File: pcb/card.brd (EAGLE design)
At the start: 84.8 x 54 mm, 22 parts, among them IC1 74HC14D, IC2 24LC256SN, Q1 BC817

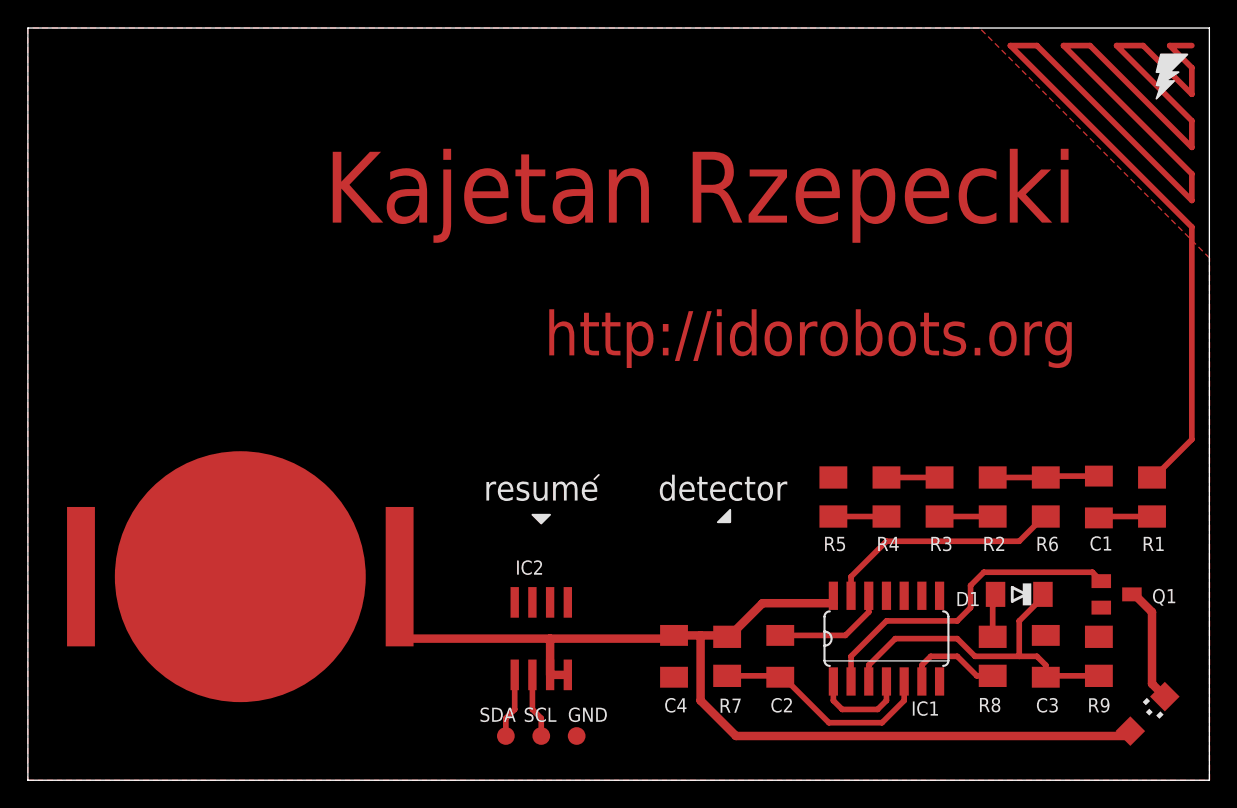
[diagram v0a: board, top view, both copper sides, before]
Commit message: Added a centigrade measure to the PCB edge.
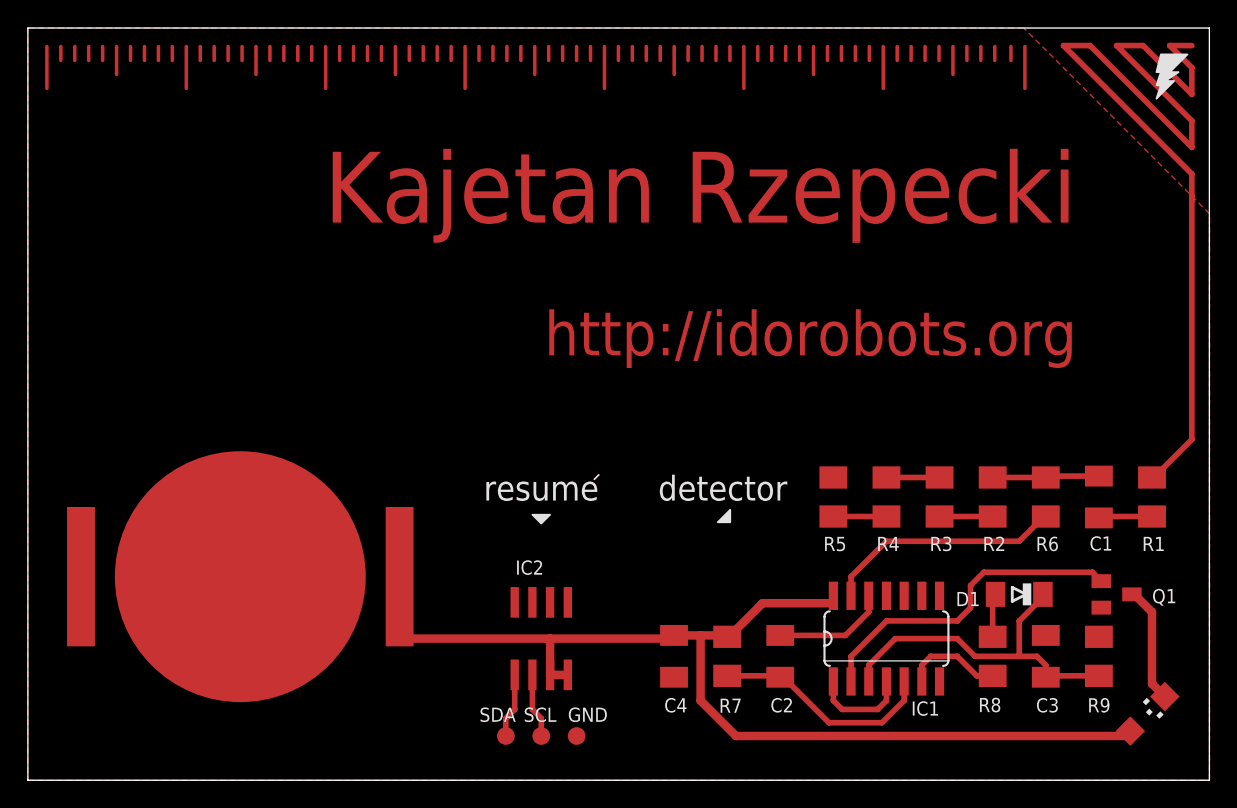
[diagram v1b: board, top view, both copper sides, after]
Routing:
- net ANT: track 104.7 -> 70.6 mm
- net N$87: track 0.00 -> 3.00 mm
- net N$77: track 0.00 -> 3.00 mm
- net N$67: track 0.00 -> 3.00 mm
- net N$57: track 0.00 -> 3.00 mm
- net N$47: track 0.00 -> 3.00 mm
- net N$37: track 0.00 -> 3.00 mm
- net N$27: track 0.00 -> 3.00 mm
- net N$17: track 0.00 -> 3.00 mm
- net N$82: track 0.00 -> 2.00 mm
- net N$72: track 0.00 -> 2.00 mm
- net N$62: track 0.00 -> 2.00 mm
- net N$52: track 0.00 -> 2.00 mm
- net N$42: track 0.00 -> 2.00 mm
- net N$32: track 0.00 -> 2.00 mm
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
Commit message: Swapped I2C EEPROM for SPI Flash & adjusted the design accordingly.
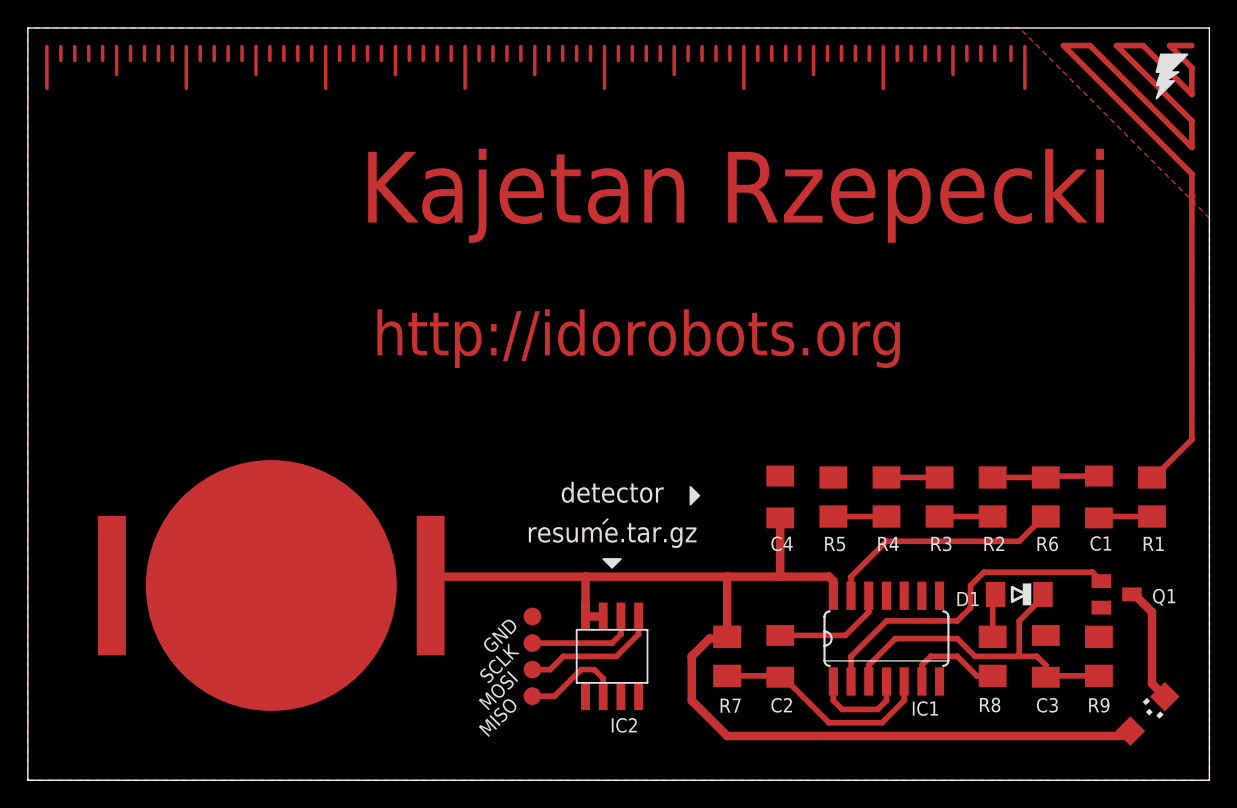
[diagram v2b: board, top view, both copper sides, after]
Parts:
- removed SCL, SDA: TPB1,27, testpad:B1,27
- added MISO, MOSI, SCLK: TPB1,27, testpad:B1,27
- IC2: value 24LC256SN -> W25X32; device microchip:SO-08 -> bat:SOIC8
- moved C4 13.7 mm to (54.0, 20.3), turned to 270 degrees
- moved GND 9.14 mm to (36.2, 11.7), turned to 90 degrees
- moved IC2 5.85 mm to (42.5, 8.89), turned to 90 degrees
- moved BAT 2.31 mm to (17.5, 14.0)
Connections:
- new net N$88: IC2.2, MISO.TP
- net GND: no longer IC2.2
- net N$10: now also IC2.6, SCLK.TP; no longer IC2.5, SDA.TP
- net N$9: now also IC2.5, MOSI.TP; no longer IC2.6, SCL.TP
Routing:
- net N$88: track 0.00 -> 7.40 mm
- net N$9: track 4.65 -> 9.94 mm
- net VCC: track 80.0 -> 83.6 mm
- net N$10: track 4.65 -> 7.88 mm
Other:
- board text added: "resume.tar.gz"
- board text removed: "resume"

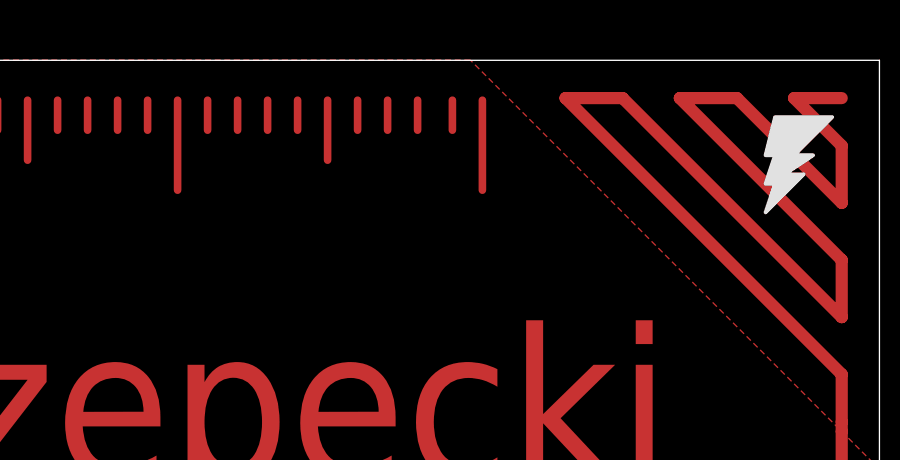
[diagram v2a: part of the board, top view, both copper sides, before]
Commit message: Fixed misaligned centigrade measure wires.
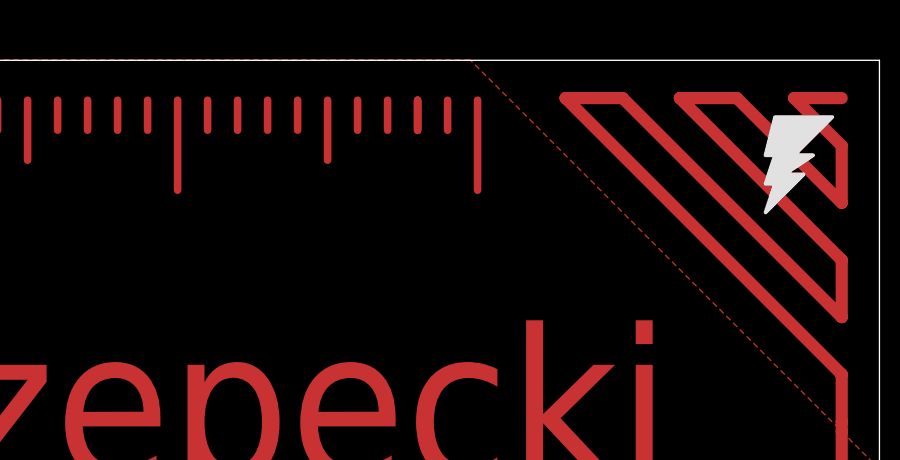
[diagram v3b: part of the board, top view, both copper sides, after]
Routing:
- net N$90: track 0.00 -> 1.00 mm
- net N$89: track 0.00 -> 1.00 mm
- net N$86: track 1.00 -> 0.00 mm
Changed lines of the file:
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@@
 <wire x1="69.365" y1="52.635" x2="69.365" y2="51.635" width="0.254" layer="1"/>
 </signal>
-<signal name="N$86">
-<wire x1="70.525" y1="52.635" x2="70.525" y2="51.635" width="0.254" layer="1"/>
-</signal>
 <signal name="N$87">
-<wire x1="71.525" y1="52.635" x2="71.525" y2="49.635" width="0.254" layer="1"/>
+<wire x1="71.36384375" y1="52.635" x2="71.36384375" y2="49.635" width="0.254" layer="1"/>
 </signal>
 <signal name="N$10">
@@
 <wire x1="37.7825" y1="6.0325" x2="36.195" y2="6.0325" width="0.4064" layer="1"/>
 </signal>
+<signal name="N$89">
+<wire x1="69.3651875" y1="52.633190625" x2="69.3651875" y2="51.633190625" width="0.254" layer="1"/>
+</signal>
+<signal name="N$90">
+<wire x1="70.3651875" y1="51.633190625" x2="70.3651875" y2="52.633190625" width="0.254" layer="1"/>
+</signal>
 </signals>

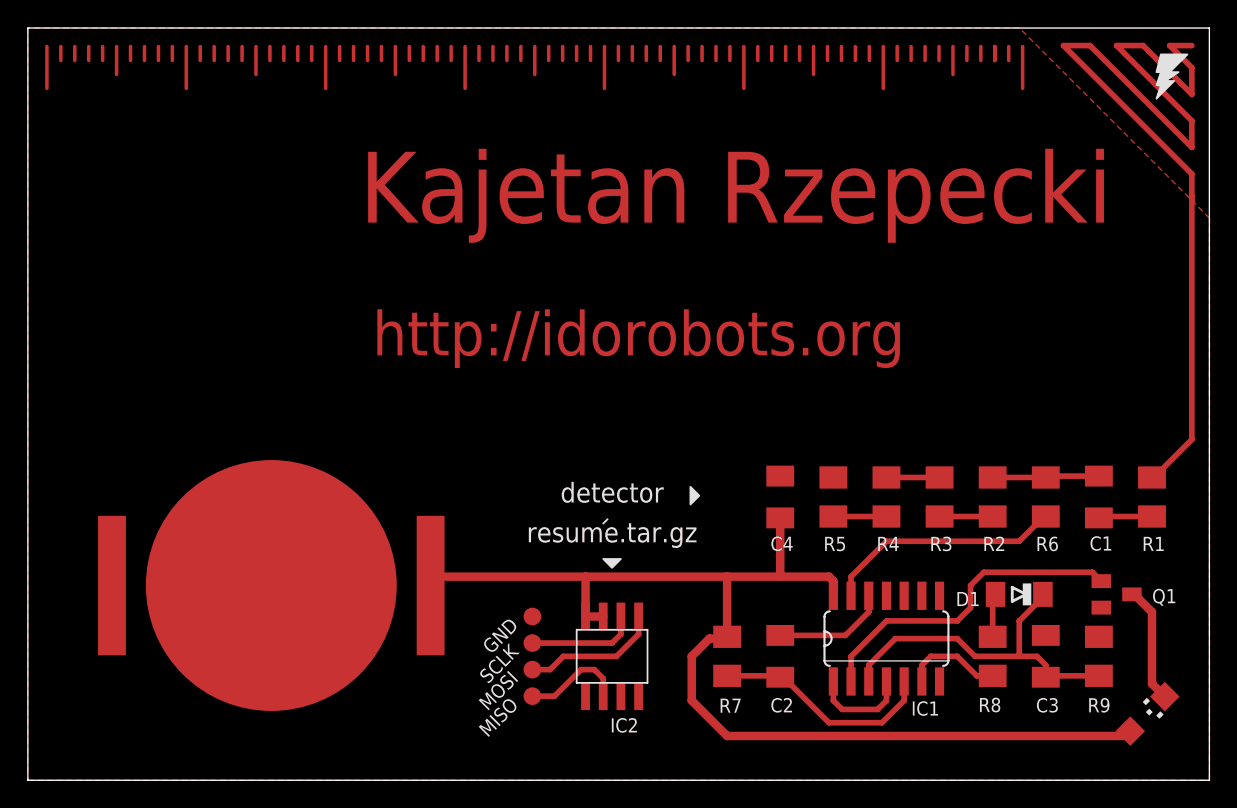
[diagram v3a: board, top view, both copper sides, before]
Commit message: Optimized the design.
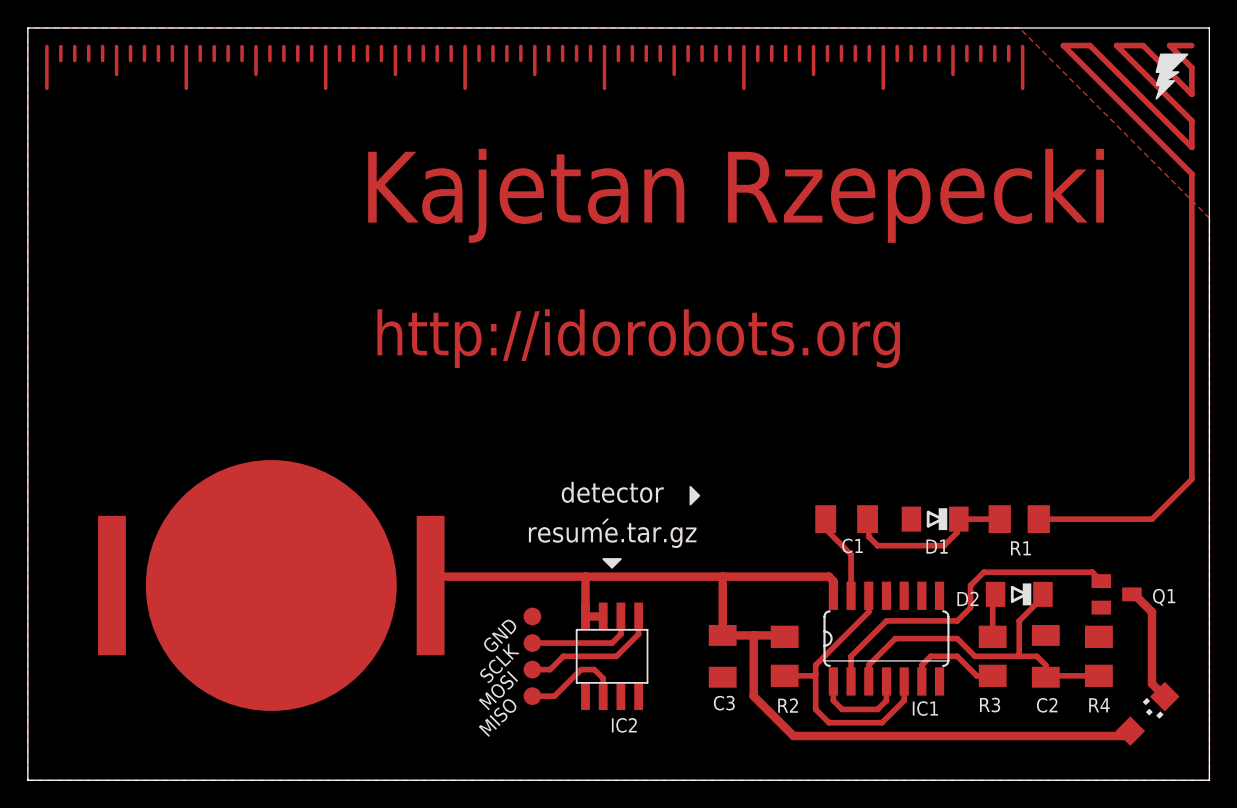
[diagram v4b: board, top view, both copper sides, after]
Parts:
- removed C4: 10nF, resistor:C1206K
- removed R5: 10M, resistor:M1206
- removed R6, R7, R9: 470k, resistor:M1206
- removed R8: 100k, resistor:M1206
- added D2: (no value), diode:MINIMELF
- R2, R4: value 10M -> 470k
- R3: value 10M -> 100k
- moved C3 23.2 mm to (49.8, 8.89)
- moved C2 19.1 mm to (73.0, 8.89)
- moved R4 19.0 mm to (76.8, 8.89)
- moved R2 18.8 mm to (54.3, 8.89)
- moved C1 18.2 mm to (58.7, 18.7), turned to 0 degrees
- moved R3 12.0 mm to (69.2, 8.89)
- moved R1 9.66 mm to (71.1, 18.7), turned to 0 degrees
- moved D1 8.09 mm to (65.1, 18.7)
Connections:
- removed net N$14: R2.1, R3.2
- removed net N$15: R3.1, R4.2
- removed net N$16: R4.1, R5.2
- removed net N$3: IC1.13, R6.1
- removed net N$4: C2.2, IC1.12
- net GND: now also C2.2, C3.1, D1.A, R4.2; no longer C3.2, C4.1, R5.1, R9.2
- net N$1: now also IC1.13; no longer R1.1
- net N$2: now also D1.C, R1.1; no longer R2.2, R6.2
- net N$5: now also IC1.12, R2.1; no longer C2.1, R7.1
- net N$6: now also R3.2; no longer R8.2
- net N$7: now also D2.A, R3.1; no longer D1.A, R8.1
- net N$8: now also C2.1, D2.C, R4.1; no longer C3.1, D1.C, R9.1
- net VCC: now also C3.2, R2.2; no longer C4.2, R7.2
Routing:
- net N$3: track 17.1 -> 0.00 mm
- net ANT: track 70.6 -> 81.4 mm
- net N$4: track 8.21 -> 0.00 mm
- net VCC: track 83.6 -> 77.7 mm
- net N$2: track 7.63 -> 12.2 mm
- net N$5: track 17.0 -> 21.3 mm
- net N$16: track 3.81 -> 0.00 mm
- net N$15: track 3.81 -> 0.00 mm
- net N$14: track 3.81 -> 0.00 mm
- net N$1: track 4.46 -> 6.25 mm
- net N$85: track 1.00 -> 0.00 mm
